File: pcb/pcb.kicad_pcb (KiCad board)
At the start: 2 copper layers, 25 parts, among them J1 Conn_02x04_Odd_Even, J10 Conn_02x04_Odd_Even, J11 Conn_02x04_Odd_Even, J12 Conn_02x04_Odd_Even, J13 Conn_02x04_Odd_Even, J14 Conn_02x04_Odd_Even, J15 Conn_02x04_Odd_Even, J16 Conn_02x04_Odd_Even, J17 Conn_02x04_Odd_Even, J18 Conn_02x04_Odd_Even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

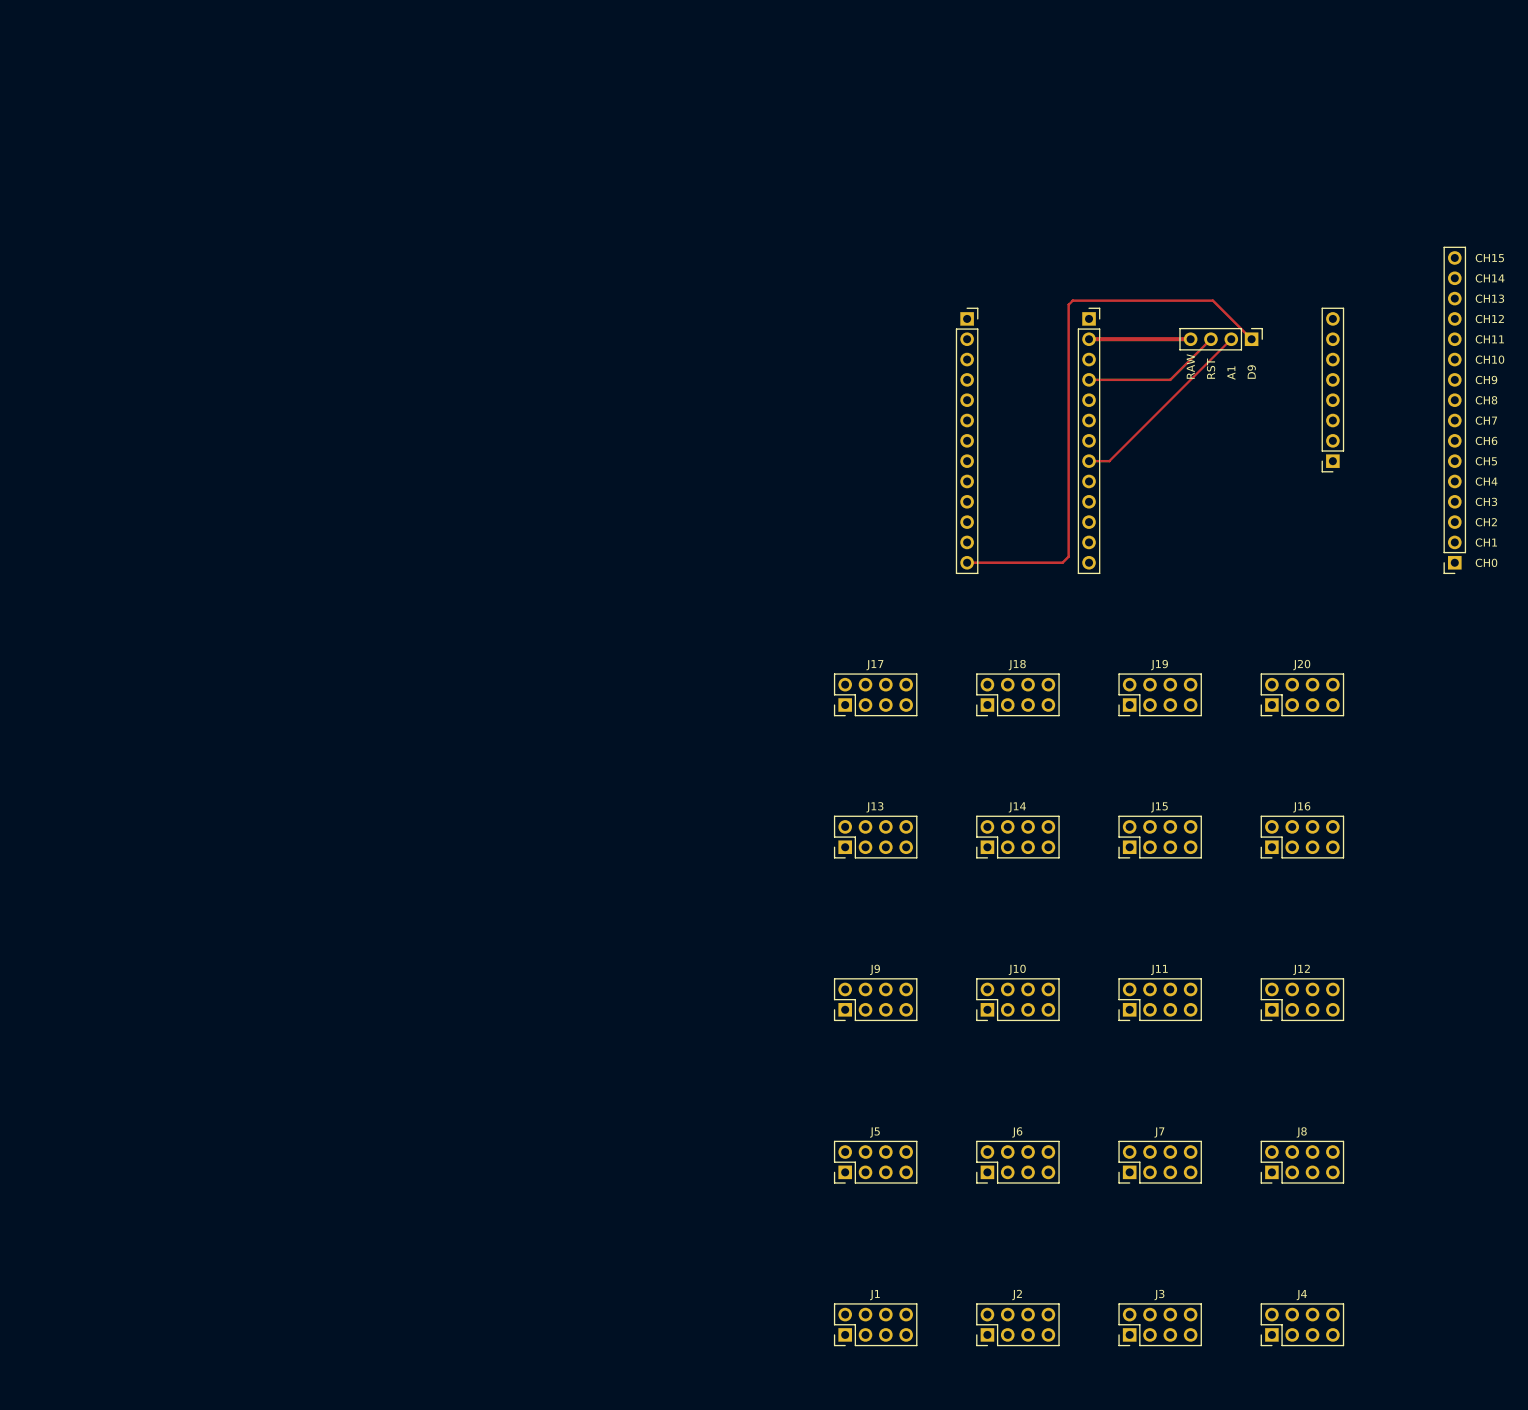
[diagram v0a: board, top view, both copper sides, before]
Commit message: pcb edge cuts
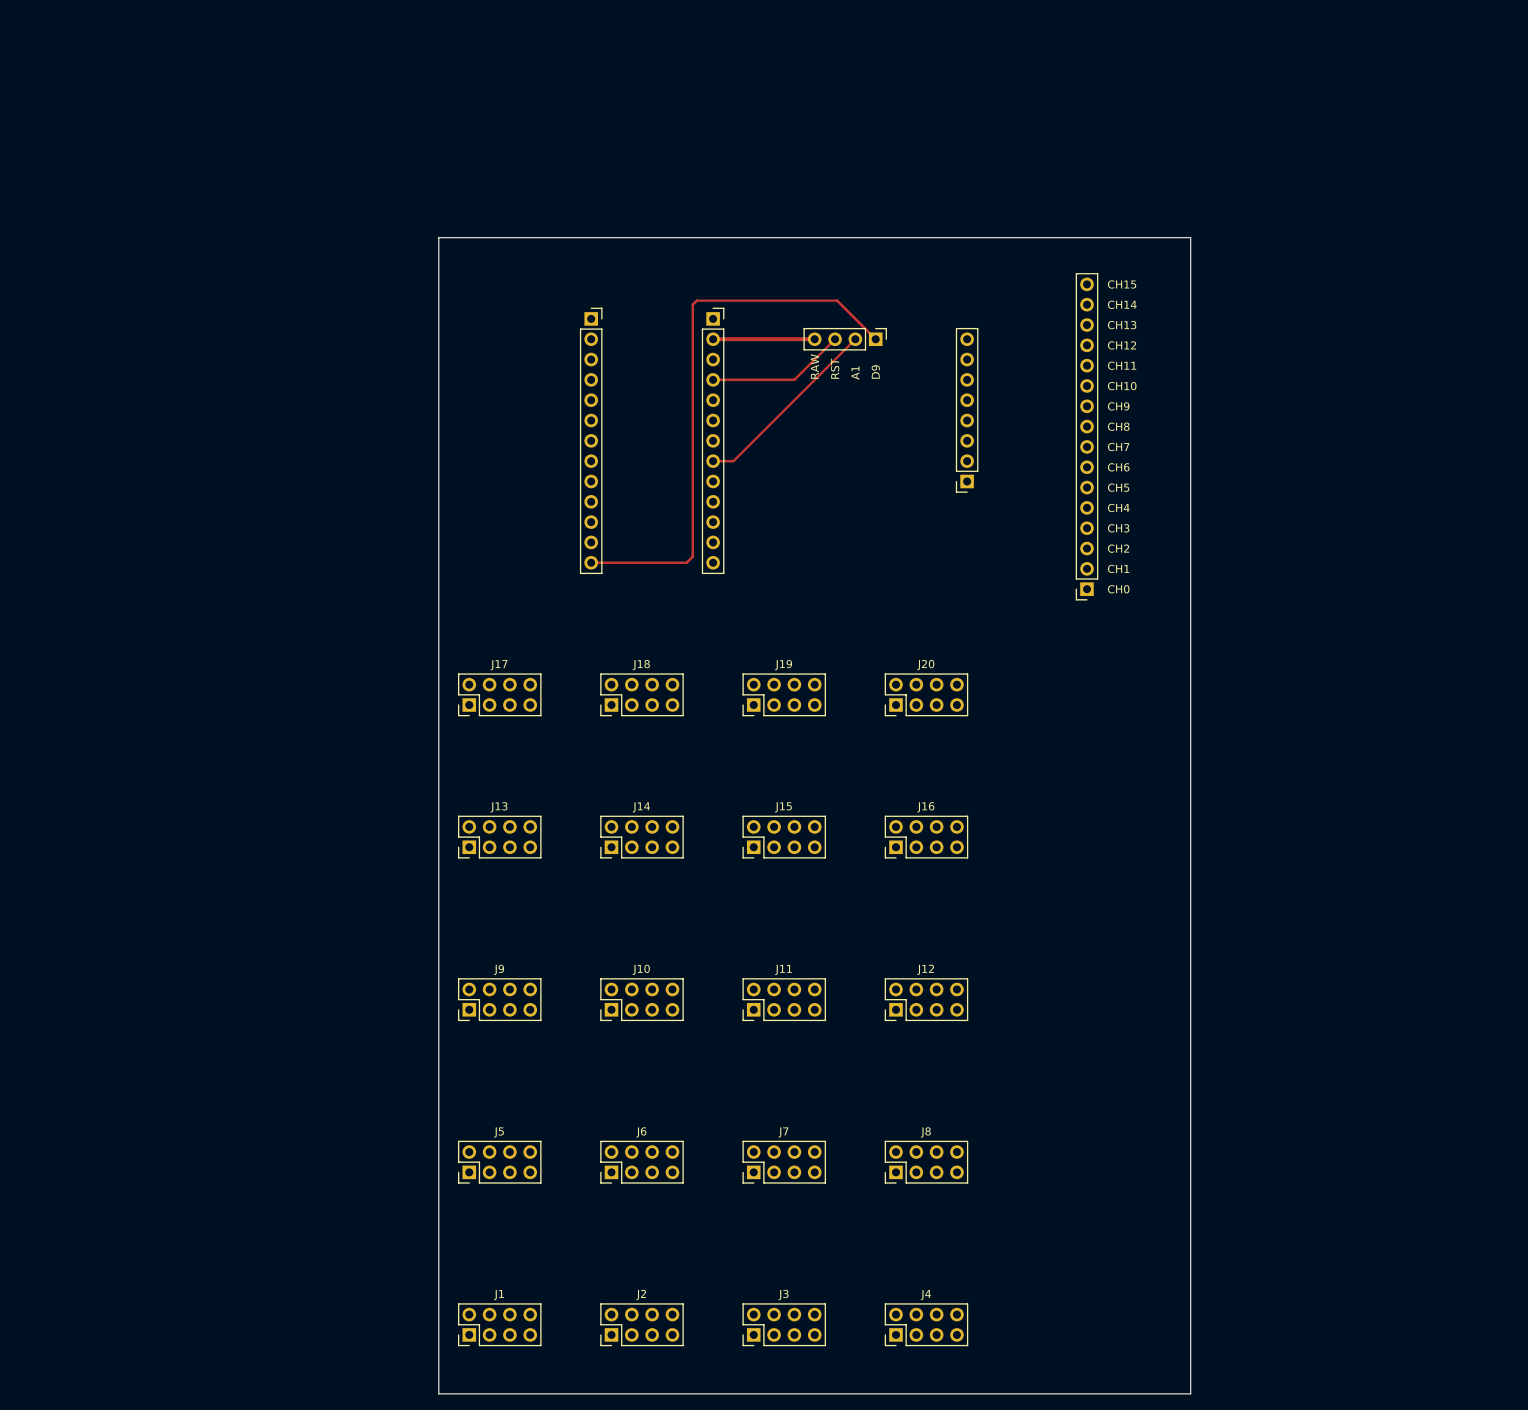
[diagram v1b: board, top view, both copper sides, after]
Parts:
- moved J21 47.0 mm to (105.4, 38.1)
- moved J22 47.0 mm to (69.8, 35.6)
- moved J23 47.0 mm to (85.1, 35.6)
- moved J1 47.0 mm to (54.6, 162.6)
- moved J10 47.0 mm to (72.4, 121.9)
- moved J11 47.0 mm to (90.2, 121.9)
- moved J12 47.0 mm to (108.0, 121.9)
- moved J13 47.0 mm to (54.6, 101.6)
- moved J14 47.0 mm to (72.4, 101.6)
- moved J15 47.0 mm to (90.2, 101.6)
- moved J16 47.0 mm to (108.0, 101.6)
- moved J17 47.0 mm to (54.6, 83.8)
- moved J18 47.0 mm to (72.4, 83.8)
- moved J19 47.0 mm to (90.2, 83.8)
- moved J2 47.0 mm to (72.4, 162.6)
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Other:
- board outline added: 94 x 144.5 mm
- rule pad_to_mask_clearance: 0 -> 0.038

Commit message: pcb component placement
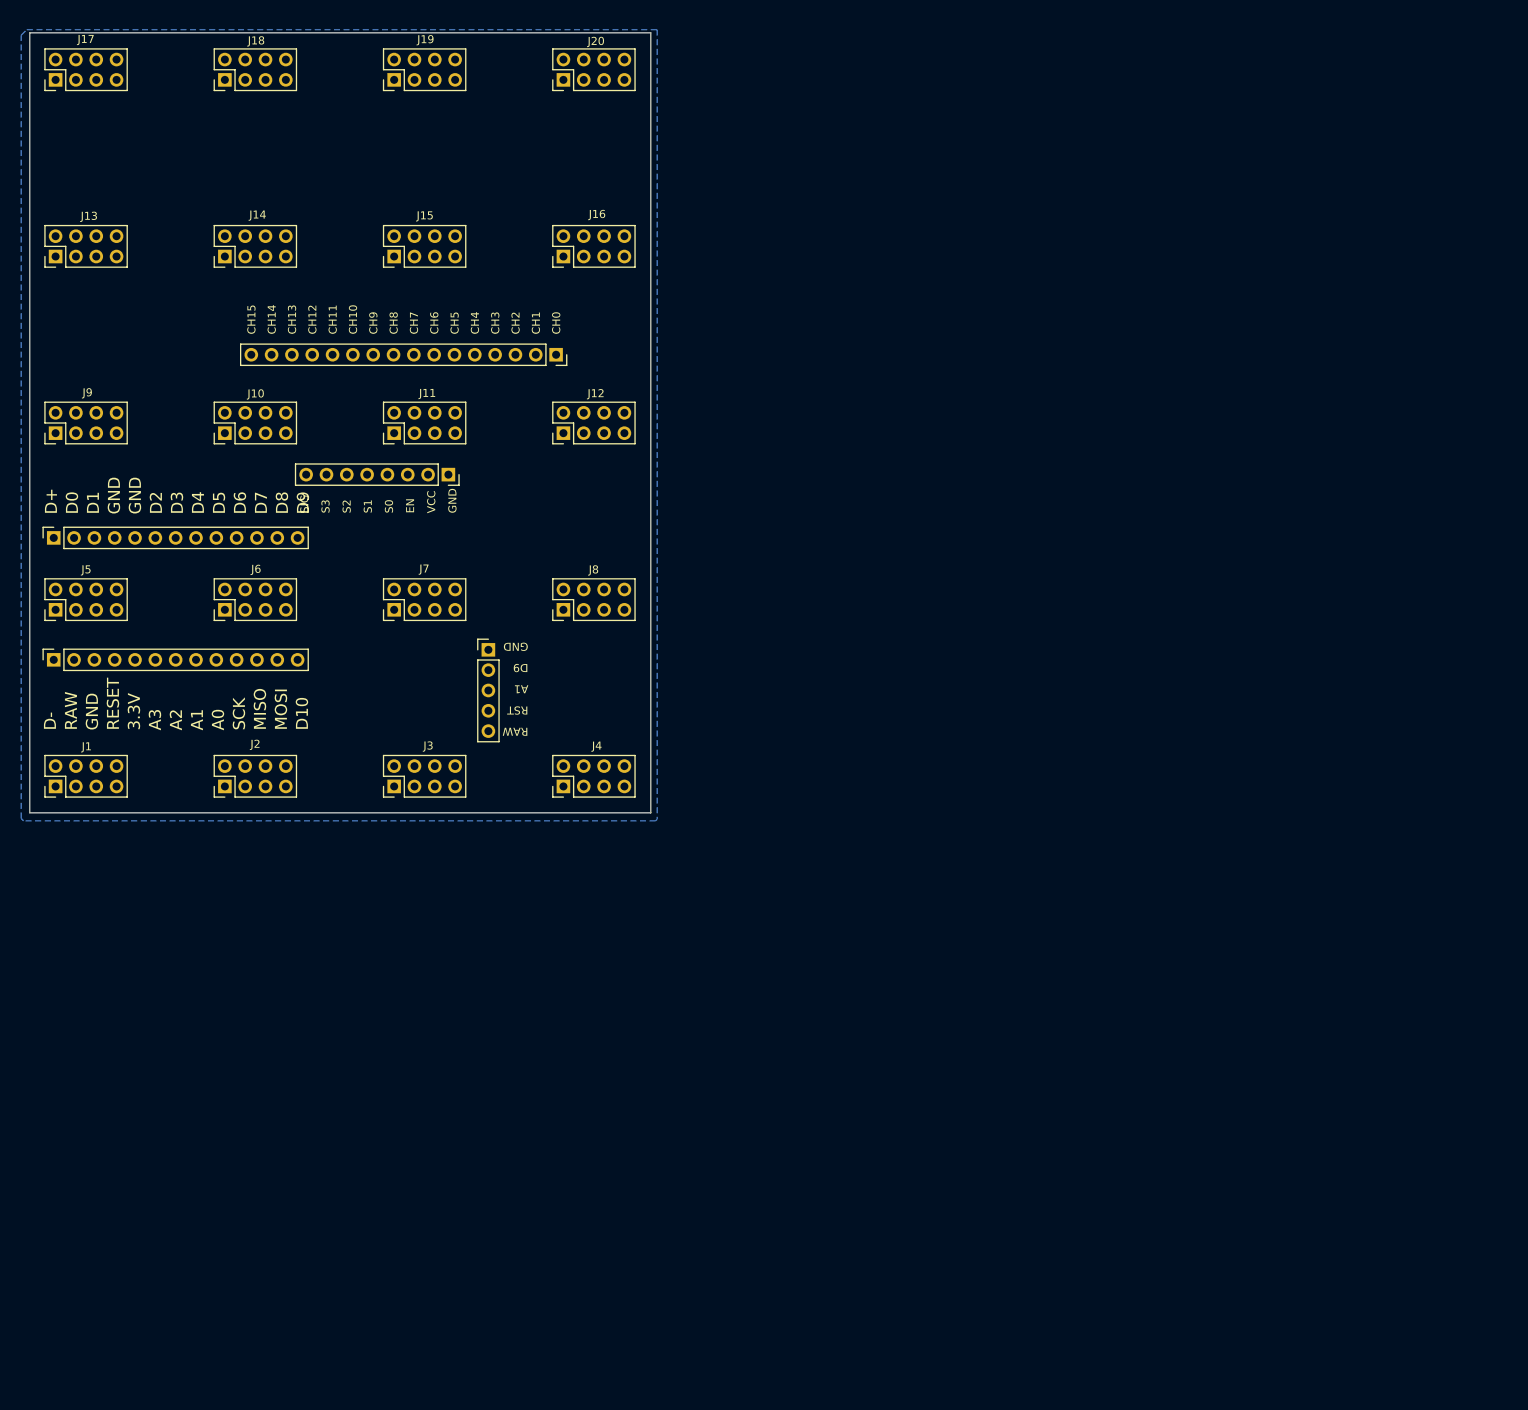
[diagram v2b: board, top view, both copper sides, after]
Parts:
- J21: value Conn_01x04_Pin -> Conn_01x05_Pin; footprint Connector_PinHeader_2.54mm:PinHeader_1x04_P2.54mm_Vertical -> Connector_PinHeader_2.54mm:PinHeader_1x05_P2.54mm_Vertical
- moved J17 93.7 mm to (2.90, 5.68)
- moved J23 92.8 mm to (2.67, 78.2), turned to 90 degrees
- moved J18 91.9 mm to (24.1, 5.68)
- moved J19 90.1 mm to (45.2, 5.68)
- moved J13 90.1 mm to (2.90, 27.8)
- moved J9 88.7 mm to (2.90, 49.8)
- moved J20 88.5 mm to (66.4, 5.68)
- moved J14 88.3 mm to (24.1, 27.8)
- moved J5 87.3 mm to (2.90, 71.9)
- moved J10 86.8 mm to (24.1, 49.8)
- moved J15 86.4 mm to (45.2, 27.8)
- moved J1 85.9 mm to (2.90, 94.0)
- moved J6 85.3 mm to (24.1, 71.9)
- moved J11 84.9 mm to (45.2, 49.8)
- moved J16 84.7 mm to (66.4, 27.8)
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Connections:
- J21 pad 1: Net-(J21-Pin_1) -> GND
- J22 pad 13: Net-(J21-Pin_1) -> Net-(J21-Pin_2)
- J23 pad 2: Net-(J21-Pin_4) -> Net-(J21-Pin_5)
- J23 pad 4: Net-(J21-Pin_3) -> Net-(J21-Pin_4)
- J23 pad 8: Net-(J21-Pin_2) -> Net-(J21-Pin_3)
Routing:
- net Net-(J21-Pin_1): track 69.6 -> 0.00 mm
- net Net-(J21-Pin_2): track 24.1 -> 0.00 mm
- net Net-(J21-Pin_3): track 17.3 -> 0.00 mm
- net Net-(J21-Pin_4): track 12.7 -> 0.00 mm
- added copper zone on B.Cu, net GND
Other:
- board size 94 x 144.5 mm -> 77.6 x 97.5 mm
- board text added: "3.3V"
- board text added: "A0"
- board text added: "A2"
- board text added: "A3"
- board text added: "D+"
- board text added: "D-"
- board text added: "D0"
- board text added: "D1"
- board text added: "D10"
- board text added: "D2"
- board text added: "D3"
- board text added: "D4"
- board text added: "D5"
- board text added: "D6"
- board text added: "D7"
- board text added: "D8"
- board text added: "EN"
- board text added: "GND"
- board text added: "MISO"
- board text added: "MOSI"
- board text added: "RESET"
- board text added: "S0"
- board text added: "S1"
- board text added: "S2"
- board text added: "S3"
- board text added: "SCK"
- board text added: "SIG"
- board text added: "USB C"
- board text added: "VCC"

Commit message: first routing design
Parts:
- moved J24 3.38 mm to (55.4, 55.0)
- moved J25 3.38 mm to (68.8, 40.0)
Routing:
- net Net-(J1-Pin_7): track 0.00 -> 469.9 mm, vias 0 -> 2
- net +3.3V: track 0.00 -> 448.4 mm, vias 0 -> 4
- net Net-(J1-Pin_8): track 0.00 -> 438.9 mm, vias 0 -> 2
- net Net-(J12-Pin_4): track 0.00 -> 163.5 mm, vias 0 -> 2
- net Net-(J1-Pin_4): track 0.00 -> 142.2 mm, vias 0 -> 5
- net Net-(J11-Pin_4): track 0.00 -> 139.7 mm, vias 0 -> 2
- net Net-(J17-Pin_6): track 0.00 -> 133.8 mm, vias 0 -> 1
- net Net-(J13-Pin_6): track 0.00 -> 114.3 mm
- net Net-(J10-Pin_4): track 0.00 -> 113.1 mm
- net Net-(J1-Pin_6): track 0.00 -> 108.1 mm
- net Net-(J10-Pin_6): track 0.00 -> 88.4 mm, vias 0 -> 2
- net Net-(J25-Pin_1): track 0.00 -> 82.8 mm
- net Net-(J22-Pin_3): track 0.00 -> 80.0 mm, vias 0 -> 4
- net GND: track 0.00 -> 75.7 mm, vias 0 -> 27
- net Net-(J25-Pin_2): track 0.00 -> 71.3 mm, vias 0 -> 1
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
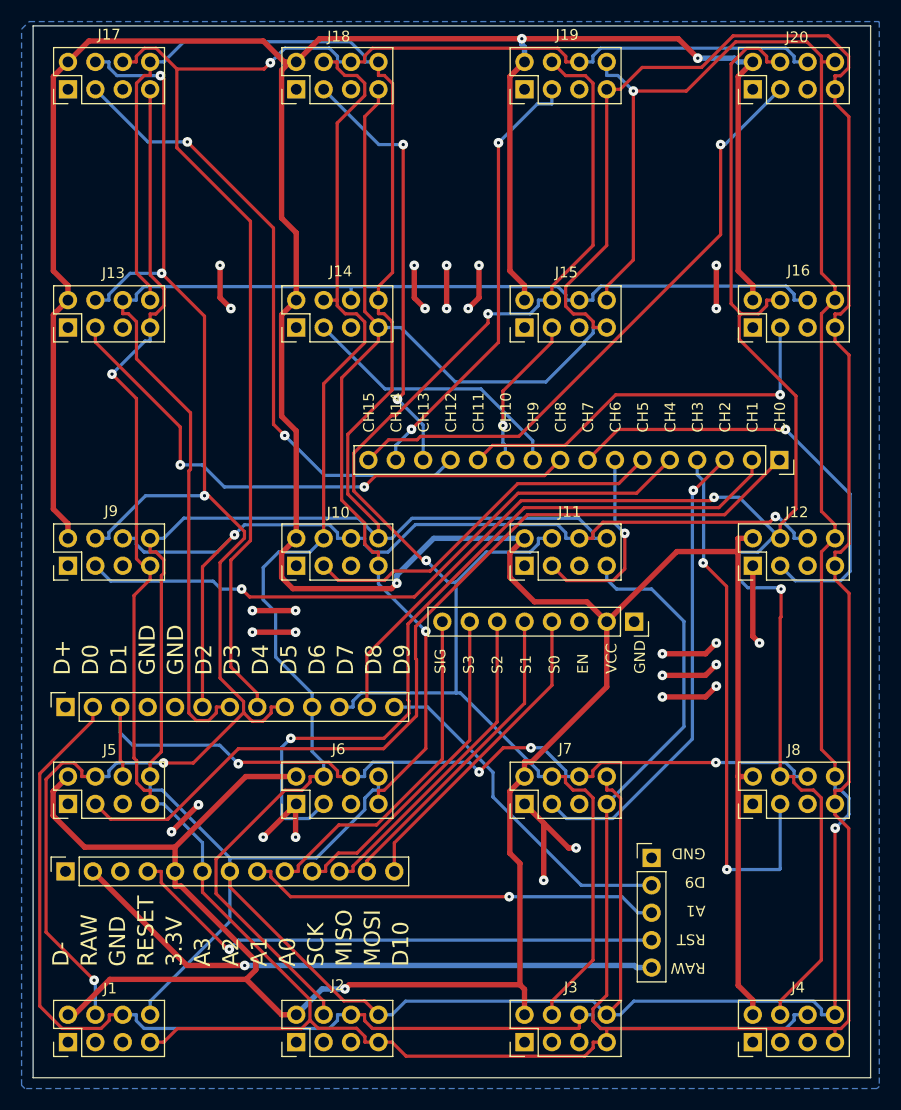
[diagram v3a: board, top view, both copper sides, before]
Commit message: pcb autosave, git ignore update
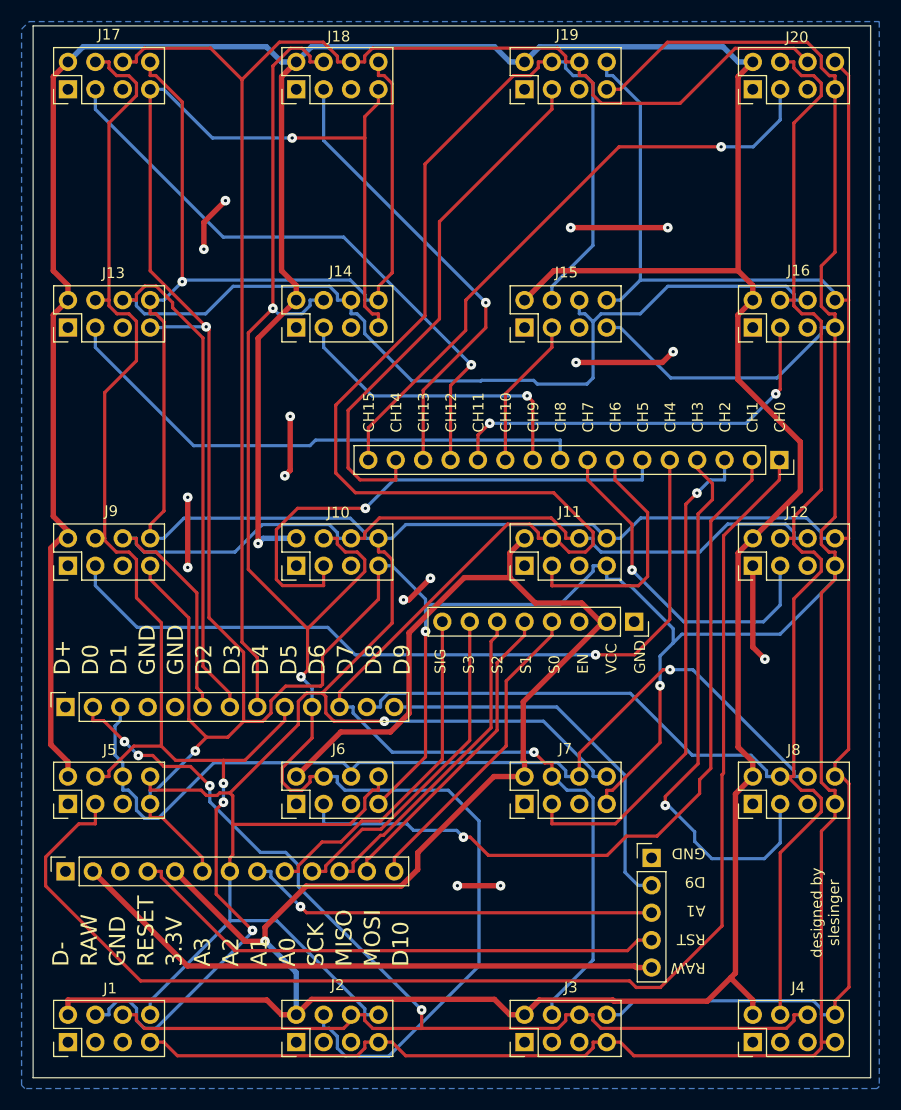
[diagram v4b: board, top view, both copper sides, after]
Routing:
- net Net-(J11-Pin_4): track 139.7 -> 184.7 mm, vias 2 -> 1
- net Net-(J25-Pin_1): track 82.8 -> 124.8 mm
- net Net-(J10-Pin_4): track 113.1 -> 152.6 mm, vias 0 -> 2
- net +3.3V: track 448.4 -> 487.7 mm, vias 4 -> 2
- net GND: track 75.7 -> 52.4 mm, vias 27 -> 15
- net Net-(J12-Pin_4): track 163.5 -> 147.8 mm, vias 2 -> 0
- net Net-(J25-Pin_5): track 59.7 -> 73.9 mm
- net Net-(J10-Pin_3): track 34.7 -> 48.8 mm, vias 0 -> 1
- net Net-(J13-Pin_6): track 114.3 -> 127.2 mm
- net Net-(J1-Pin_8): track 438.9 -> 451.5 mm
- net Net-(J12-Pin_3): track 42.6 -> 31.9 mm
- net Net-(J1-Pin_7): track 469.9 -> 479.0 mm, vias 2 -> 5
- net Net-(J19-Pin_3): track 41.1 -> 49.6 mm, vias 2 -> 0
- net Net-(J22-Pin_3): track 80.0 -> 87.4 mm, vias 4 -> 1
- net Net-(J1-Pin_6): track 108.1 -> 115.4 mm, vias 0 -> 4
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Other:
- board text added: "designed by slesinger"
